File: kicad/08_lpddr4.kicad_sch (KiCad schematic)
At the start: 37 parts, among them U501 Ti135N484I3, U801 H9HCNNN8KUMLHR-NME

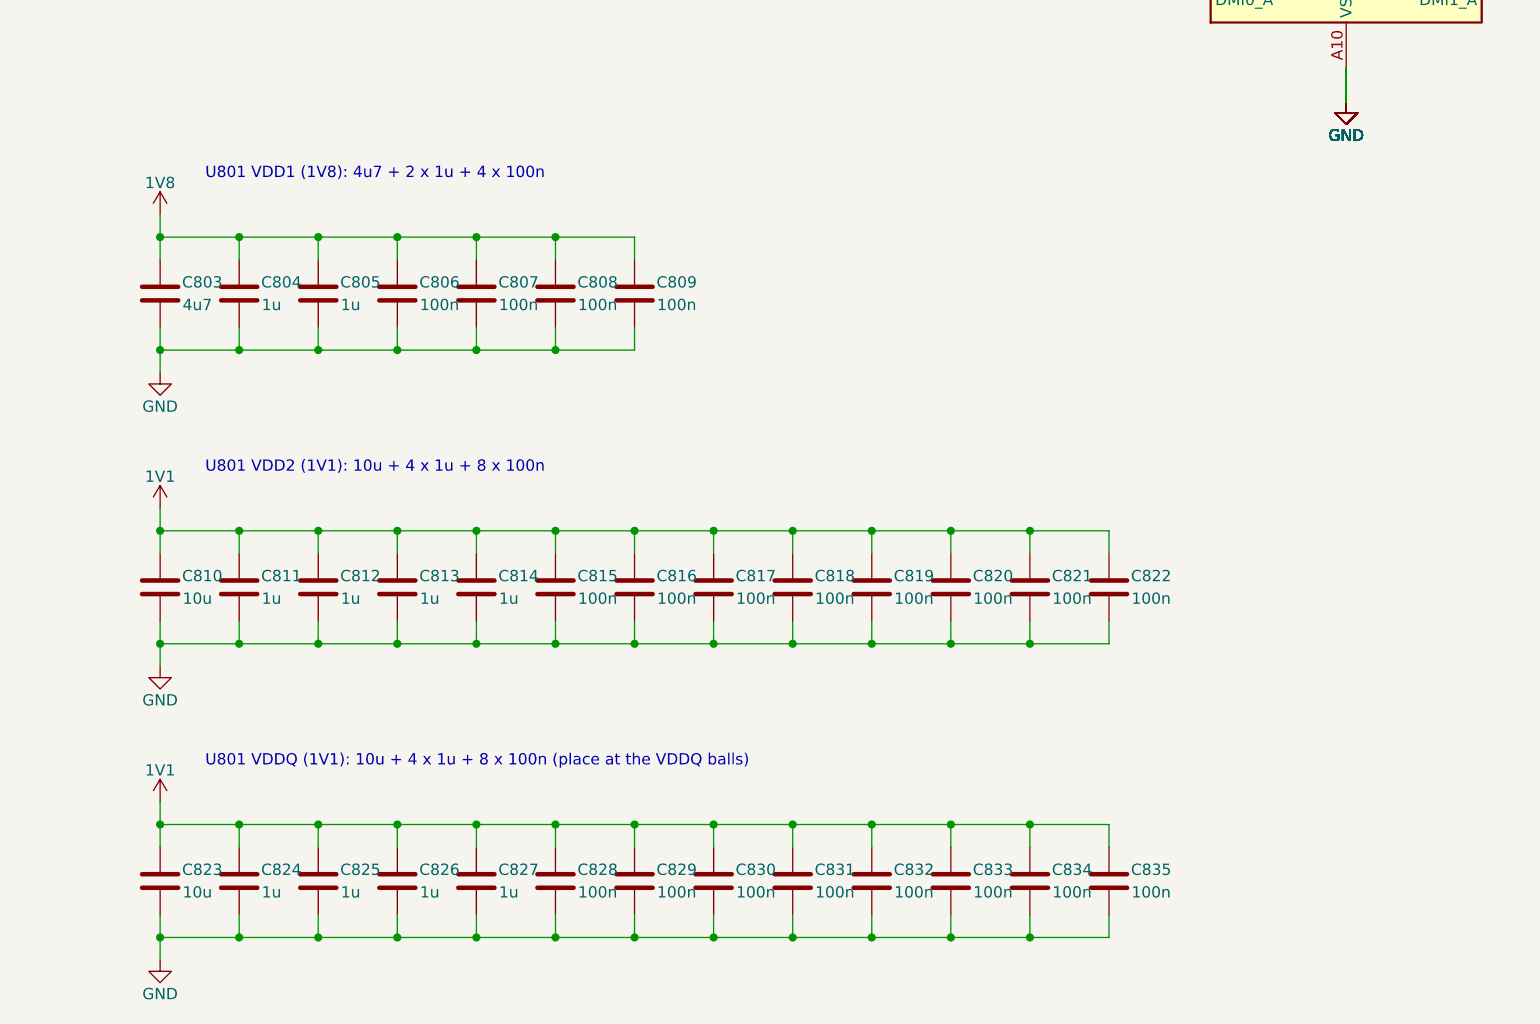
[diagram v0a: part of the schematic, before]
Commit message: break out top row dq
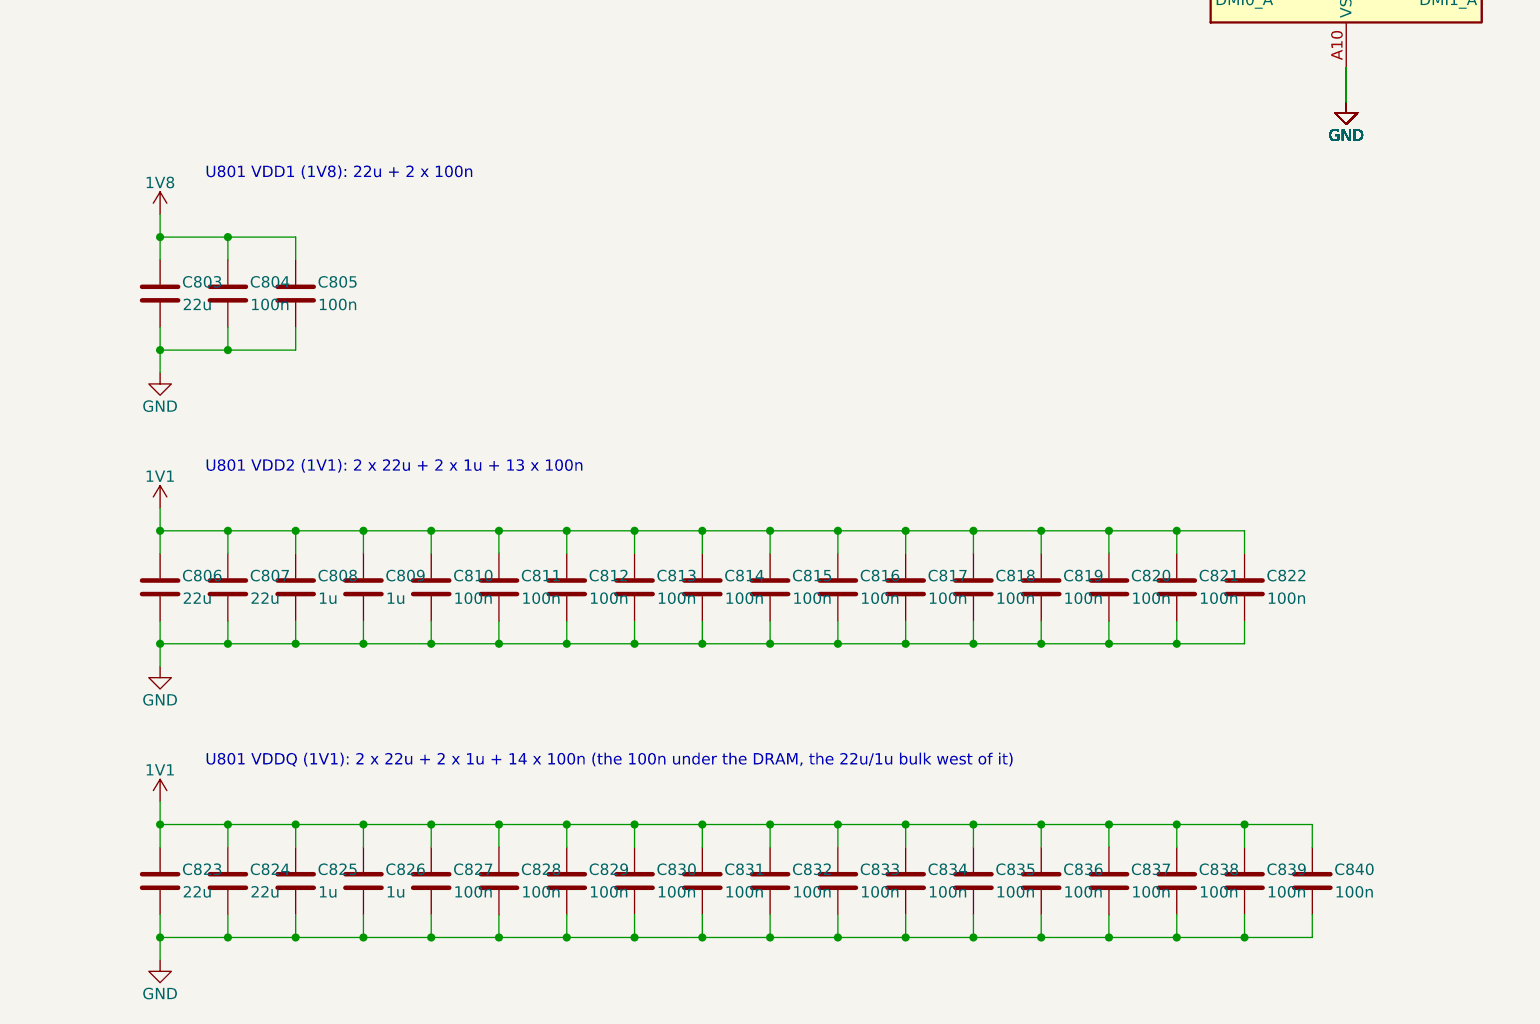
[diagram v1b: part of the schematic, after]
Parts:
- added C836, C837, C838, C839, C840: 100n, Capacitor_SMD:C_0201_0603Metric, symbol ti135_card:C
- C803: value 4u7 -> 22u; LCSC (none) -> C415703
- C804, C805, C811, C812, C813, C814, C827: value 1u -> 100n; footprint Capacitor_SMD:C_0402_1005Metric -> Capacitor_SMD:C_0201_0603Metric; LCSC (none) -> C190183
- C806, C807: value 100n -> 22u; LCSC (none) -> C415703
- C808, C809: value 100n -> 1u; LCSC (none) -> C52923
- C810: value 10u -> 100n; footprint Capacitor_SMD:C_0805_2012Metric -> Capacitor_SMD:C_0201_0603Metric; LCSC (none) -> C190183
- C815, C816, C817, C818, C819, C820, C821, C822, C828, C829, C830, C831, C832, C833, C834, C835: footprint Capacitor_SMD:C_0402_1005Metric -> Capacitor_SMD:C_0201_0603Metric; LCSC (none) -> C190183
- C823: value 10u -> 22u; footprint Capacitor_SMD:C_0805_2012Metric -> Capacitor_SMD:C_0402_1005Metric; LCSC (none) -> C415703
- C824: value 1u -> 22u; LCSC (none) -> C415703
- C825, C826: LCSC (none) -> C52923
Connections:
- net 1V1: now also C806.1, C807.1, C808.1, C809.1, C836.1, C837.1, C838.1, C839.1, C840.1
- net 1V8: no longer C806.1, C807.1, C808.1, C809.1
- net GND: now also C836.2, C837.2, C838.2, C839.2, C840.2
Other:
- note added: "U801 VDD1 (1V8): 22u + 2 x 100n"
- note added: "U801 VDD2 (1V1): 2 x 22u + 2 x 1u + 13 x 100n"
- note added: "U801 VDDQ (1V1): 2 x 22u + 2 x 1u + 14 x 100n (the 100n under the DRAM, the 22u/1u bulk west of it)"
- note removed: "U801 VDD1 (1V8): 4u7 + 2 x 1u + 4 x 100n"
- note removed: "U801 VDD2 (1V1): 10u + 4 x 1u + 8 x 100n"
- note removed: "U801 VDDQ (1V1): 10u + 4 x 1u + 8 x 100n (place at the VDDQ balls)"
- moved on the sheet: C804, C805, C806, C807, C808, C809, C810, C811, C812, C813, C814, C815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
